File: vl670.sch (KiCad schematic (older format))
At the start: 69 parts, among them J1 Conn_01x07_Male, J2 USB3_B, J3 Conn_01x08_Male, J4 USB3_A Receptacle, J5 Conn_01x02_Male, U2 VL670, U4 TPS2061C-PXLI, Y1 25MHz

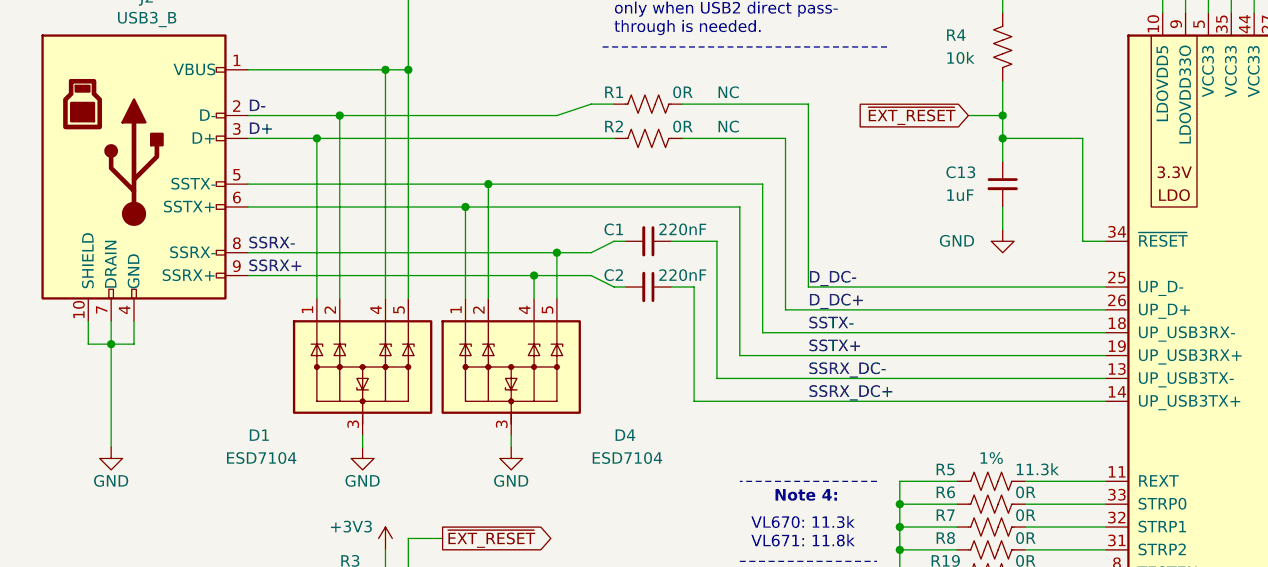
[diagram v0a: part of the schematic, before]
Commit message: fix incorrect RX/TX pairs
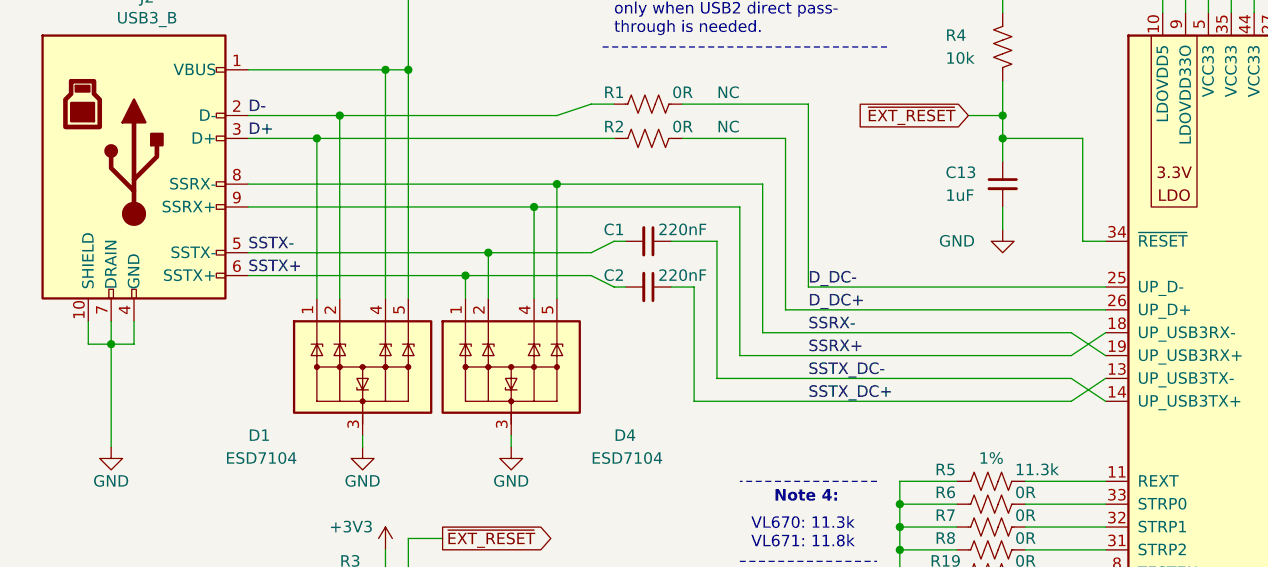
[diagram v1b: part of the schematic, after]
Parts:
- removed J2: USB3_B, vl670:USB3_B_XKB_U235-091N-4BLRC16-4-5, symbol Connector:USB3_B
- added J2: USB3_B, vl670:USB3_B_XKB_U235-091N-4BLRC16-4-5, symbol vl670:USB3_B
- renumbered C2 to C1, C1 to C2
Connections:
- net +5VP: now also J2.1 (VBUS)
- net D+: now also J2.3 (D+)
- net D-: now also J2.2 (D-)
- net GND: now also J2.10 (SHIELD), J2.4 (GND), J2.7 (DRAIN)
- net SSRX+: now also U2.18 (UP_USB3RX-), J2.9 (SSRX+); no longer C1.2
- net SSRX-: now also U2.19 (UP_USB3RX+), J2.8 (SSRX-); no longer C2.2
- net SSTX+: now also C2.2, J2.6 (SSTX+); no longer U2.19 (UP_USB3RX+)
- net SSTX-: now also C1.2, J2.5 (SSTX-); no longer U2.18 (UP_USB3RX-)
- net SSRX_DC+ renamed SSTX_DC-
- net SSRX_DC- renamed SSTX_DC+
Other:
- moved on the sheet: C1, C2
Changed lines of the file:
@@
 	3400 2300 3950 2300
 Text Label 3950 3500 0    50   ~ 0
-SSRX_DC-
+SSTX_DC-
 Text Label 3950 3600 0    50   ~ 0
-SSRX_DC+
+SSTX_DC+
 Text Label 3950 3100 0    50   ~ 0
 D_DC-
@@
 	9100 3500 9100 3550
 Text Label 3950 3400 0    50   ~ 0
-SSTX+
+SSRX+
 Text Label 3950 3300 0    50   ~ 0
-SSTX-
+SSRX-
 Text Label 3950 3200 0    50   ~ 0
 D_DC+
@@
 Text Notes 900  6750 0    50   ~ 0
 close to VL670, one per pin
-Wire Wire Line
-	3750 3300 5250 3300
-Wire Wire Line
-	3650 3400 5250 3400
 $Comp
 L Device:C_Small C11
@@
 Wire Notes Line
 	4300 600  4300 1250
-$Comp
-L Connector:USB3_B J2
-U 1 1 617F0239
-P 1000 2550
-F 0 "J2" H 1057 3267 50  0000 C CNN
-F 1 "USB3_B" H 1057 3176 50  0000 C CNN
-F 2 "vl670:USB3_B_XKB_U235-091N-4BLRC16-4-5" H 1150 2650 50  0001 C CNN
-F 3 "~" H 1150 2650 50  0001 C CNN
-	1    1000 2550
-	1    0    0    -1
-$EndComp
 Wire Wire Line
 	3000 2300 2850 2350
@@
 	1000 3350 900  3350
 Text Label 1500 2950 0    50   ~ 0
-SSRX-
+SSTX-
 Text Label 1500 3050 0    50   ~ 0
-SSRX+
+SSTX+
 Wire Wire Line
 	2200 800  2200 850
@@
 	3450 3100 3350 3100
 $Comp
+L Device:C_Small C2
+U 1 1 6188E9E7
+P 3250 3100
+AR Path="/6188E9E7" Ref="C2"  Part="1"
+AR Path="/60085564/6188E9E7" Ref="C?"  Part="1"
+F 0 "C2" V 3200 2950 50  0000 C CNN
+F 1 "220nF" V 3200 3250 50  0000 C CNN
+F 2 "Capacitor_SMD:C_0603_1608Metric_Pad1.08x0.95mm_HandSolder" H 3250 3100 50  0001 C CNN
+F 3 "~" H 3250 3100 50  0001 C CNN
+	1    3250 3100
+	0    1    1    0
+$EndComp
+$Comp
 L Device:C_Small C1
-U 1 1 6188E9E7
+U 1 1 6188E9E1
 P 3250 2900
-AR Path="/6188E9E7" Ref="C1"  Part="1"
-AR Path="/60085564/6188E9E7" Ref="C?"  Part="1"
+AR Path="/6188E9E1" Ref="C1"  Part="1"
+AR Path="/60085564/6188E9E1" Ref="C?"  Part="1"
 F 0 "C1" V 3200 2750 50  0000 C CNN
 F 1 "220nF" V 3200 3050 50  0000 C CNN
@@
 	0    1    1    0
 $EndComp
-$Comp
-L Device:C_Small C2
-U 1 1 6188E9E1
-P 3250 3100
-AR Path="/6188E9E1" Ref="C2"  Part="1"
-AR Path="/60085564/6188E9E1" Ref="C?"  Part="1"
-F 0 "C2" V 3200 2950 50  0000 C CNN
-F 1 "220nF" V 3200 3250 50  0000 C CNN
-F 2 "Capacitor_SMD:C_0603_1608Metric_Pad1.08x0.95mm_HandSolder" H 3250 3100 50  0001 C CNN
-F 3 "~" H 3250 3100 50  0001 C CNN
-	1    3250 3100
-	0    1    1    0
-$EndComp
 Wire Wire Line
 	3000 2950 3100 2900
 Wire Wire Line
 	3000 3050 3100 3100
-Wire Wire Line
-	3550 3500 5250 3500
-Wire Wire Line
-	3450 3600 5250 3600
 $Comp
 L vl670:ESD7104 D1
@@
 Wire Wire Line
 	1800 3150 1800 2450
-Wire Wire Line
-	2550 3150 2550 2650
-Wire Wire Line
-	2450 3150 2450 2750
-Wire Wire Line
-	2850 3150 2850 2950
-Wire Wire Line
-	2750 3150 2750 3050
 Connection ~ 2100 2150
 Connection ~ 1800 2450
@@
 Wire Wire Line
 	1900 2350 2850 2350
-Connection ~ 2450 2750
-Wire Wire Line
-	2450 2750 3650 2750
-Connection ~ 2550 2650
-Wire Wire Line
-	2550 2650 3750 2650
-Connection ~ 2750 3050
-Wire Wire Line
-	2750 3050 3000 3050
-Connection ~ 2850 2950
-Wire Wire Line
-	2850 2950 3000 2950
-Wire Wire Line
-	1500 2950 2850 2950
-Wire Wire Line
-	1500 3050 2750 3050
-Wire Wire Line
-	1500 2650 2550 2650
-Wire Wire Line
-	1500 2750 2450 2750
 Wire Wire Line
 	1500 2450 1800 2450
@@
 Wire Wire Line
 	2200 2150 2200 3150
+$Comp
+L vl670:USB3_B J2
+U 1 1 61885314
+P 1000 2550
+F 0 "J2" H 1057 3267 50  0000 C CNN
+F 1 "USB3_B" H 1057 3176 50  0000 C CNN
+F 2 "vl670:USB3_B_XKB_U235-091N-4BLRC16-4-5" H 1150 2650 50  0001 C CNN
+F 3 "~" H 1150 2650 50  0001 C CNN
+	1    1000 2550
+	1    0    0    -1
+$EndComp
+Wire Wire Line
+	1500 3050 2450 3050
+Wire Wire Line
+	1500 2650 2850 2650
+Wire Wire Line
+	1500 2750 2750 2750
+Wire Wire Line
+	2450 3150 2450 3050
+Connection ~ 2450 3050
+Wire Wire Line
+	2550 3150 2550 2950
+Wire Wire Line
+	1500 2950 2550 2950
+Connection ~ 2550 2950
+Wire Wire Line
+	2450 3050 3000 3050
+Wire Wire Line
+	2550 2950 3000 2950
+Wire Wire Line
+	2750 3150 2750 2750
+Connection ~ 2750 2750
+Wire Wire Line
+	2750 2750 3650 2750
+Wire Wire Line
+	2850 3150 2850 2650
+Connection ~ 2850 2650
+Wire Wire Line
+	2850 2650 3750 2650
+Wire Wire Line
+	3550 3500 5100 3500
+Wire Wire Line
+	3450 3600 5100 3600
+Wire Wire Line
+	5100 3600 5250 3500
+Wire Wire Line
+	5100 3500 5250 3600
+Wire Wire Line
+	3750 3300 5100 3300
+Wire Wire Line
+	3650 3400 5100 3400
+Wire Wire Line
+	5100 3300 5250 3400
+Wire Wire Line
+	5100 3400 5250 3300
 $EndSCHEMATC

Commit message: misc modifications.
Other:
- moved on the sheet: R1
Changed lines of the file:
@@
 L Device:R_US R1
 U 1 1 6027A505
-P 3250 2300
-F 0 "R1" V 3200 2150 50  0000 C CNN
-F 1 "0R" V 3200 2450 50  0000 C CNN
-F 2 "Resistor_SMD:R_0603_1608Metric_Pad0.98x0.95mm_HandSolder" V 3290 2290 50  0001 C CNN
-F 3 "~" H 3250 2300 50  0001 C CNN
-F 4 "NC" V 3200 2650 50  0000 C CNN "Install"
-	1    3250 2300
+P 3250 2350
+F 0 "R1" V 3200 2200 50  0000 C CNN
+F 1 "0R" V 3200 2500 50  0000 C CNN
+F 2 "Resistor_SMD:R_0603_1608Metric_Pad0.98x0.95mm_HandSolder" V 3290 2340 50  0001 C CNN
+F 3 "~" H 3250 2350 50  0001 C CNN
+F 4 "NC" V 3200 2700 50  0000 C CNN "Install"
+	1    3250 2350
 	0    1    1    0
 $EndComp
@@
 	3850 3200 5250 3200
 Wire Wire Line
-	3950 2300 3950 3100
-Wire Wire Line
 	3950 3100 5250 3100
 Wire Wire Line
-	3000 2300 3100 2300
-Wire Wire Line
 	3400 2450 3850 2450
-Wire Wire Line
-	3400 2300 3950 2300
 Text Label 3950 3500 0    50   ~ 0
 SSTX_DC-
@@
 	950  1050 1150 1050
 Connection ~ 1150 1050
-Wire Notes Line
-	700  600  4300 600
-Wire Notes Line
-	700  1250 4300 1250
 Wire Wire Line
 	6500 1900 6500 1800
@@
 Wire Wire Line
 	3000 850  3200 850
-Text Notes 3800 750  0    50   ~ 10
+Text Notes 3700 800  0    50   ~ 10
 Note 2:
-Text Notes 3400 1100 0    50   ~ 0
+Text Notes 3400 1150 0    50   ~ 0
 Cut JP2 to isolate USB\nconnector from global 5 V\nrail for debugging with\nexternal power.
 Wire Wire Line
@@
 	700  600  700  1250
 Wire Notes Line
-	4300 600  4300 1250
-Wire Wire Line
-	3000 2300 2850 2350
+	4500 600  4500 1250
 $Comp
 L power:GND #PWR0107
@@
 Connection ~ 1900 2350
 Wire Wire Line
-	1900 2350 2850 2350
-Wire Wire Line
 	1500 2450 1800 2450
 Wire Wire Line
@@
 Wire Wire Line
 	5100 3400 5250 3300
+Wire Notes Line
+	700  1250 4500 1250
+Wire Notes Line
+	700  600  4500 600
+Wire Wire Line
+	1900 2350 3100 2350
+Wire Wire Line
+	3400 2350 3950 2350
+Wire Wire Line
+	3950 2350 3950 3100
 $EndSCHEMATC
